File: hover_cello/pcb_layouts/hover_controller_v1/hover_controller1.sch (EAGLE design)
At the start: 6 parts

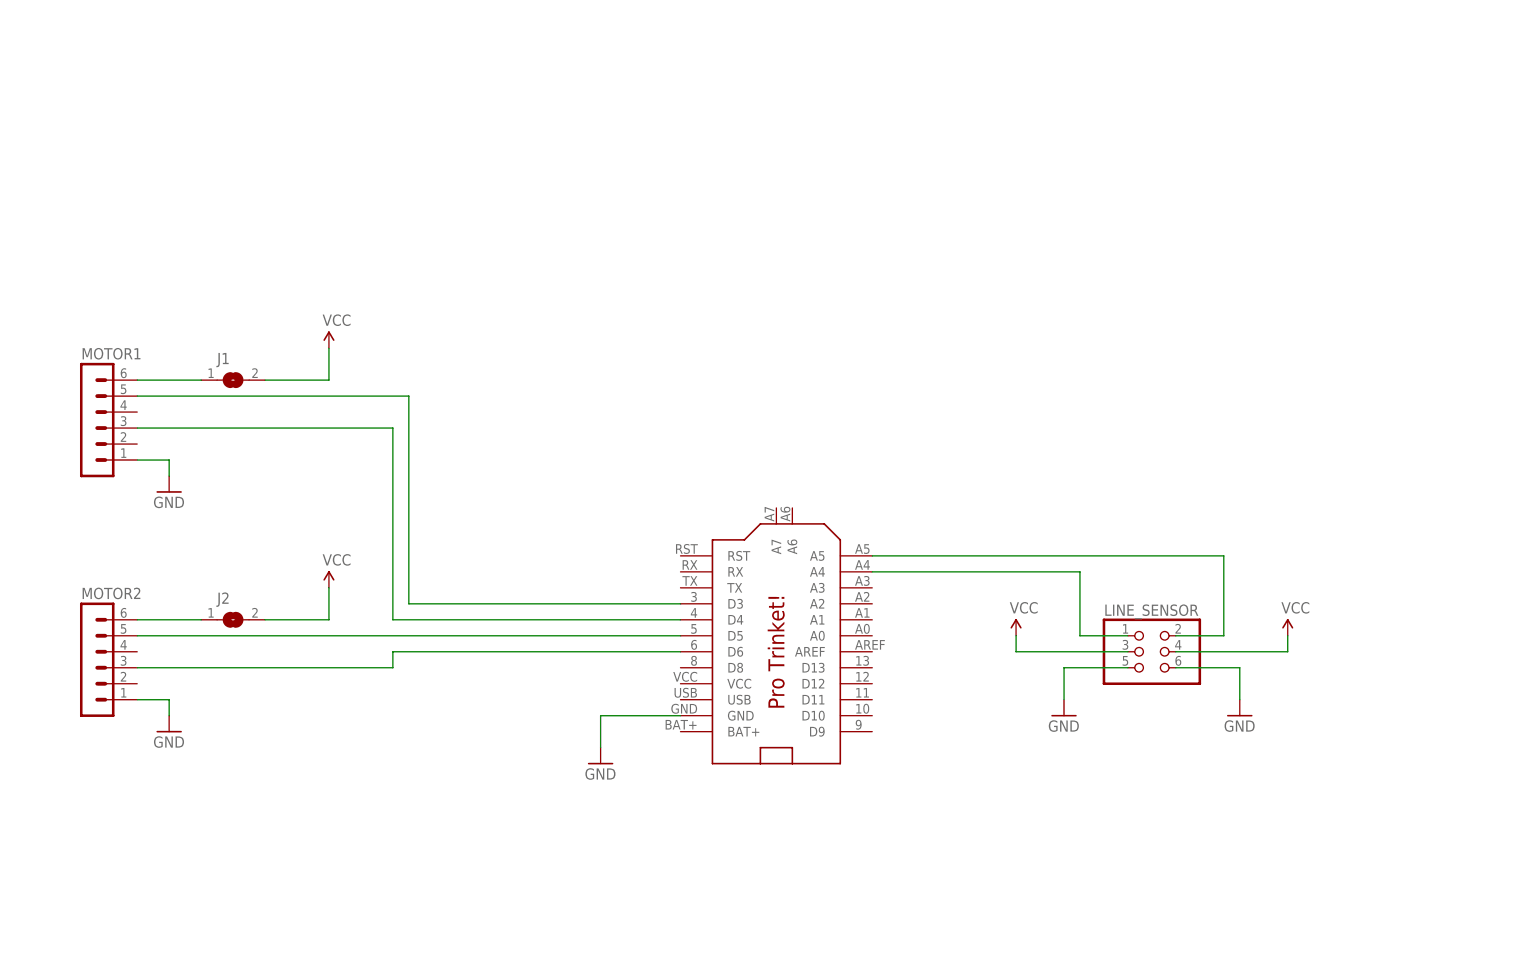
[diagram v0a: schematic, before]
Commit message: fixed annoying line not found bug, added delay on startup
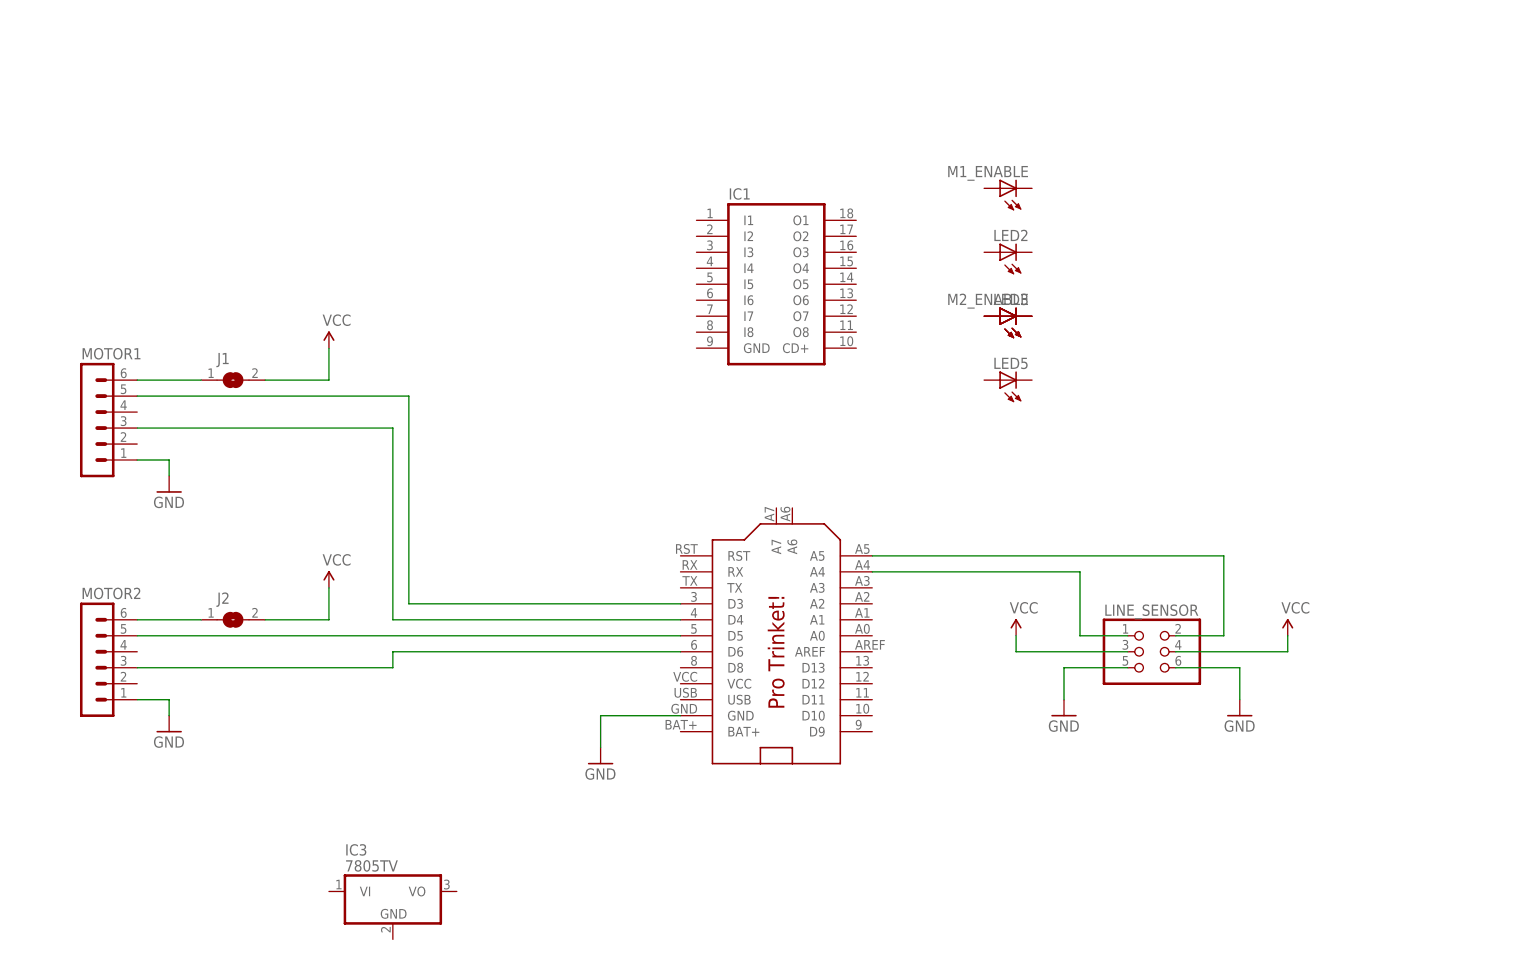
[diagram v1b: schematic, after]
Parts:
- added IC1: (no value), uln-udn:ULN2803A
- added IC3: 7805TV, linear:7805TV
- added LED2, LED3, LED5, M1_ENABLE, M2_ENABLE: (no value), led:LED3MM
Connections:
- new net N$3: LED3.C, M2_ENABLE.C
- new net N$4: LED3.A, M2_ENABLE.A
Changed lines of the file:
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@@
 <setting verticaltext="up"/>
 </settings>
-<grid distance="0.1" unitdist="inch" unit="inch" style="lines" multiple="1" display="no" altdistance="0.01" altunitdist="inch" altunit="inch"/>
+<grid distance="0.1" unitdist="inch" unit="inch" style="lines" multiple="1" display="yes" altdistance="0.01" altunitdist="inch" altunit="inch"/>
 <layers>
 <layer number="1" name="Top" color="4" fill="1" visible="no" active="no"/>
@@
 <part name="GND4" library="SparkFun-Aesthetics" deviceset="GND" device=""/>
 <part name="GND5" library="SparkFun-Aesthetics" deviceset="GND" device=""/>
+<part name="IC3" library="linear" deviceset="78*" device="TV" technology="05"/>
+<part name="IC1" library="uln-udn" library_urn="urn:adsk.eagle:library:407" deviceset="ULN2803A" device=""/>
+<part name="M1_ENABLE" library="led" library_urn="urn:adsk.eagle:library:259" deviceset="LED" device="3MM"/>
+<part name="LED2" library="led" library_urn="urn:adsk.eagle:library:259" deviceset="LED" device="3MM"/>
+<part name="LED3" library="led" library_urn="urn:adsk.eagle:library:259" deviceset="LED" device="3MM"/>
+<part name="M2_ENABLE" library="led" library_urn="urn:adsk.eagle:library:259" deviceset="LED" device="3MM"/>
+<part name="LED5" library="led" library_urn="urn:adsk.eagle:library:259" deviceset="LED" device="3MM"/>
 </parts>
 <sheets>
@@
 <instance part="GND4" gate="1" x="33.02" y="104.14"/>
 <instance part="GND5" gate="1" x="33.02" y="66.04"/>
+<instance part="IC3" gate="A1" x="68.58" y="40.64"/>
+<instance part="IC1" gate="G$1" x="129.54" y="137.16"/>
+<instance part="M1_ENABLE" gate="G$1" x="165.1" y="152.4" rot="R90"/>
+<instance part="LED2" gate="G$1" x="165.1" y="142.24" rot="R90"/>
+<instance part="LED3" gate="G$1" x="165.1" y="132.08" rot="R90"/>
+<instance part="M2_ENABLE" gate="G$1" x="165.1" y="132.08" rot="R90"/>
+<instance part="LED5" gate="G$1" x="165.1" y="121.92" rot="R90"/>
 </instances>
 <busses>
@@
 </segment>
 </net>
+<net name="N$3" class="0">
+<segment>
+<pinref part="M2_ENABLE" gate="G$1" pin="C"/>
+<pinref part="LED3" gate="G$1" pin="C"/>
+</segment>
+</net>
+<net name="N$4" class="0">
+<segment>
+<pinref part="M2_ENABLE" gate="G$1" pin="A"/>
+<pinref part="LED3" gate="G$1" pin="A"/>
+</segment>
+</net>
 </nets>
 </sheet>
@@
 </schematic>
 </drawing>
+<compatibility>
+<note version="8.2" severity="warning">
+Since Version 8.2, Eagle supports online libraries. The ids
+of those online libraries will not be understood (or retained)
+with this version.
+</note>
+</compatibility>
 </eagle>

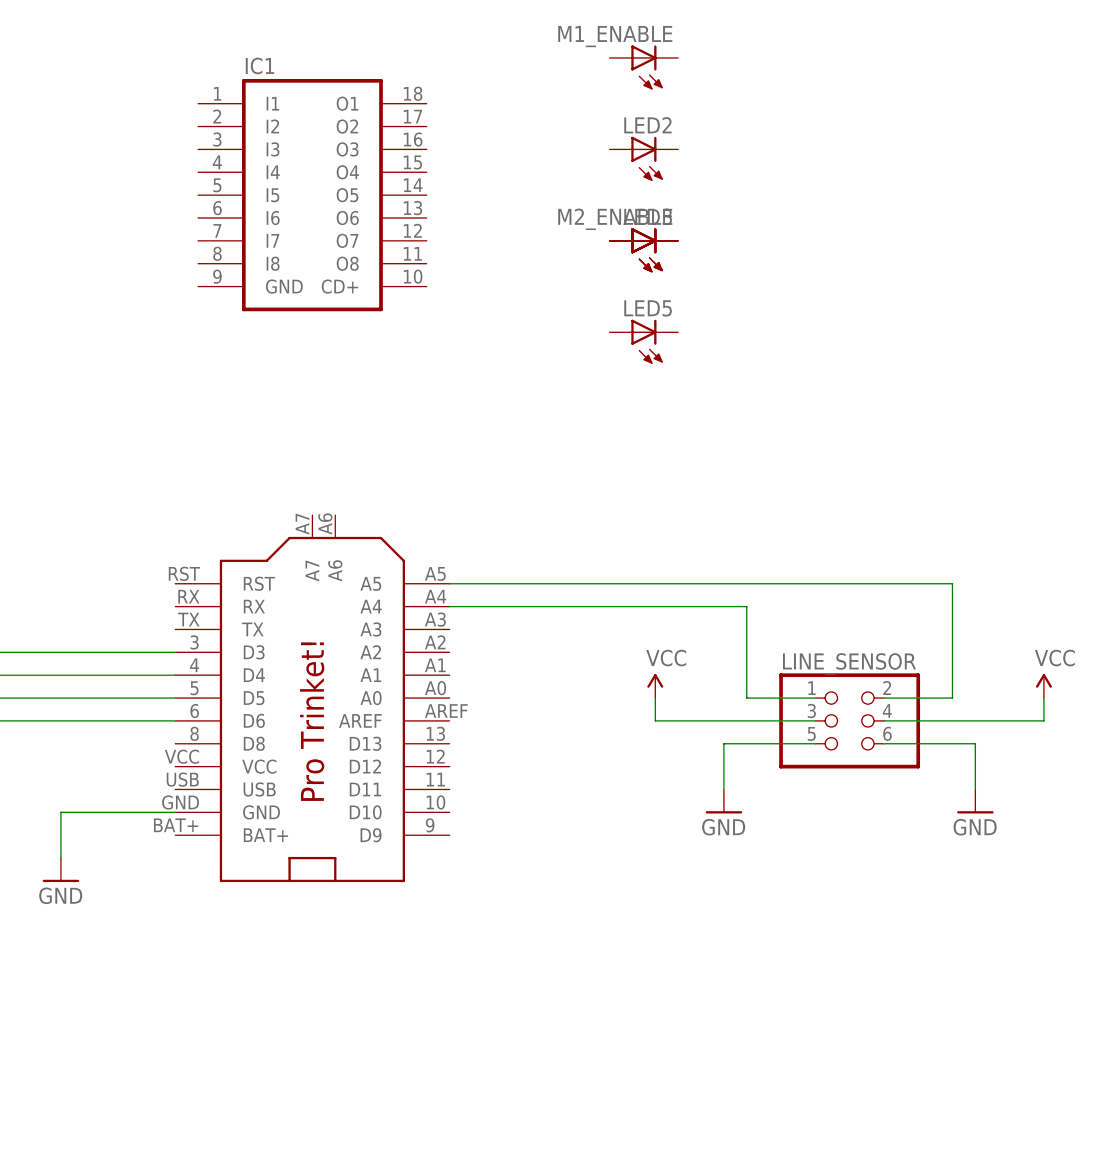
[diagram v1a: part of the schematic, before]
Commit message: added L298 DC motor driver to Eagle schematic
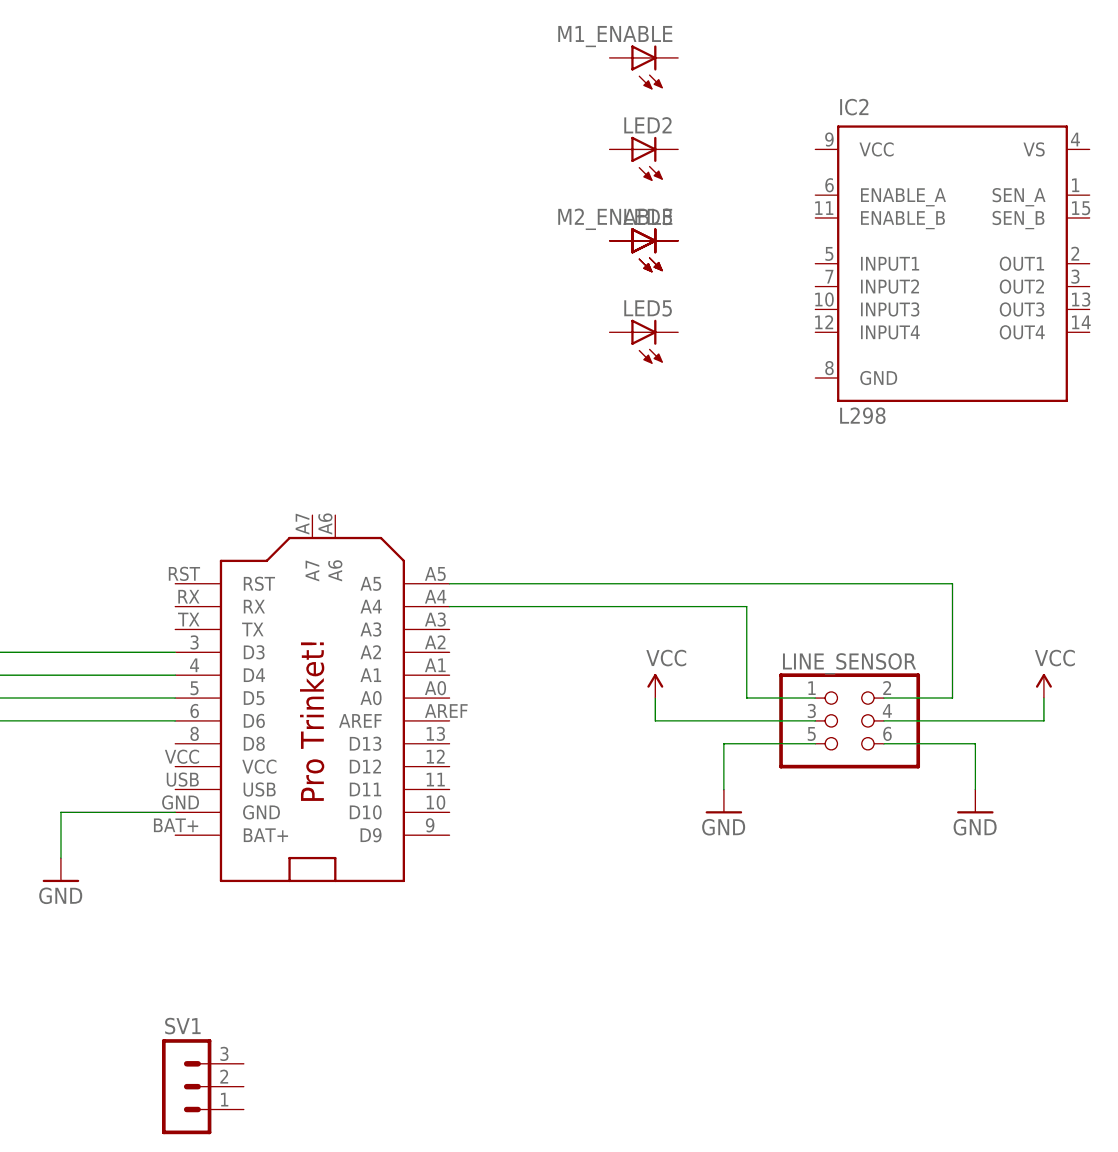
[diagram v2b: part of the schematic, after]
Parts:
- removed IC1: (no value), uln-udn:ULN2803A
- added IC2: L298, st-microelectronics:L298
- added SV1: (no value), con-lstb:MA03-1
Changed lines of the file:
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@@
 <part name="GND5" library="SparkFun-Aesthetics" deviceset="GND" device=""/>
 <part name="IC3" library="linear" deviceset="78*" device="TV" technology="05"/>
-<part name="IC1" library="uln-udn" library_urn="urn:adsk.eagle:library:407" deviceset="ULN2803A" device=""/>
 <part name="M1_ENABLE" library="led" library_urn="urn:adsk.eagle:library:259" deviceset="LED" device="3MM"/>
 <part name="LED2" library="led" library_urn="urn:adsk.eagle:library:259" deviceset="LED" device="3MM"/>
@@
 <part name="M2_ENABLE" library="led" library_urn="urn:adsk.eagle:library:259" deviceset="LED" device="3MM"/>
 <part name="LED5" library="led" library_urn="urn:adsk.eagle:library:259" deviceset="LED" device="3MM"/>
+<part name="IC2" library="st-microelectronics" deviceset="L298" device=""/>
+<part name="SV1" library="con-lstb" deviceset="MA03-1" device=""/>
 </parts>
 <sheets>
@@
 <instance part="GND5" gate="1" x="33.02" y="66.04"/>
 <instance part="IC3" gate="A1" x="68.58" y="40.64"/>
-<instance part="IC1" gate="G$1" x="129.54" y="137.16"/>
 <instance part="M1_ENABLE" gate="G$1" x="165.1" y="152.4" rot="R90"/>
 <instance part="LED2" gate="G$1" x="165.1" y="142.24" rot="R90"/>
@@
 <instance part="M2_ENABLE" gate="G$1" x="165.1" y="132.08" rot="R90"/>
 <instance part="LED5" gate="G$1" x="165.1" y="121.92" rot="R90"/>
+<instance part="IC2" gate="L298" x="200.66" y="127"/>
+<instance part="SV1" gate="G$1" x="114.3" y="38.1"/>
 </instances>
 <busses>
